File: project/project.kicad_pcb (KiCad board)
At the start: 2 copper layers, 84 x 84 mm, 155 parts, among them J101 OUT, J102 IN, J103 FFC, J104 Back, J105 Front, J301 5V, J302 24V, J303 3V3, J401 USB_C_Receptacle_USB2.0, Q101 DTC143Z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

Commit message: routing somewhat done
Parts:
- added C203: 10u/50v, Capacitor_SMD:C_0805_2012Metric_Pad1.18x1.45mm_HandSolder, F.Cu at (190.7, 103.3)
- added C205: 10u/50v, Capacitor_SMD:C_0805_2012Metric_Pad1.18x1.45mm_HandSolder, F.Cu at (139.3, 104.6)
- H101, H102: footprint MountingHole:MountingHole_3.2mm_M3_Pad_Via -> -local:MountingHole_3.2mm_M3_Pad_Via
- moved C202 55.2 mm to (188.5, 84.5), turned to -90 degrees
- moved U102 55.0 mm to (140.5, 135.6), turned to 90 degrees
- moved C201 53.3 mm to (180.5, 81.7), turned to 90 degrees
- moved R406 52.8 mm to (180.1, 140.2), turned to -90 degrees
- moved C102 52.7 mm to (143.2, 135.8), turned to -90 degrees
- moved U101 34.1 mm to (157.1, 97.6), turned to 180 degrees
- moved C101 33.5 mm to (153.9, 97.6), turned to -90 degrees
- moved kibuzzard-67570608 28.7 mm to (168.5, 122.8)
- moved R404 24.8 mm to (158.7, 124.0), turned to -90 degrees
- moved U201 19.3 mm to (194.8, 86.2), turned to 90 degrees
- moved R401 18.1 mm to (154.3, 124.0), turned to -90 degrees
- moved R402 12.4 mm to (156.3, 124.0), turned to -90 degrees
- moved R407 12.0 mm to (198.3, 125.2), turned to 90 degrees
- moved kibuzzard-66DA8205 11.4 mm to (144.3, 151.0)
- moved C204 11.0 mm to (137.9, 86.2), turned to -90 degrees
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- renumbered C203 to C204
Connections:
- C102 pad 2: B_GND -> F_GND
- C303 pad 2: B_GND -> F_GND
- C304 pad 2: B_GND -> F_GND
- C305 pad 2: B_GND -> F_GND
- C306 pad 2: B_GND -> F_GND
- C307 pad 2: B_GND -> F_GND
- C308 pad 2: B_GND -> F_GND
- C309 pad 2: B_GND -> F_GND
- C310 pad 2: B_GND -> F_GND
- C313 pad 2: B_GND -> F_GND
- C314 pad 2: B_GND -> F_GND
- C315 pad 2: B_GND -> F_GND
- C316 pad 2: B_GND -> F_GND
- C401 pad 1: B_GND -> F_GND
- C402 pad 1: B_GND -> F_GND
- C403 pad 2: B_GND -> F_GND
- C404 pad 2: B_GND -> F_GND
- C405 pad 2: B_GND -> F_GND
- C406 pad 2: B_GND -> F_GND
- C407 pad 2: B_GND -> F_GND
- C408 pad 2: B_GND -> F_GND
- C409 pad 1: B_GND -> F_GND
- C410 pad 1: B_GND -> F_GND
- C411 pad 2: B_GND -> F_GND
- C412 pad 2: B_GND -> F_GND
- C413 pad 2: B_GND -> F_GND
- H101 pad 1: unconnected-(H101-Pad1) -> F_GND
- H102 pad 1: unconnected-(H102-Pad1) -> F_GND
- H103 pad 1: unconnected-(H103-Pad1) -> F_GND
- H104 pad 1: unconnected-(H104-Pad1) -> F_GND
- J101 pad 2: B_GND -> F_GND
- J102 pad 2: B_GND -> F_GND
- J103 pad MP: GND -> F_GND
- J104 pad 1: unconnected-(J104-Pad1) -> B_SDA
- J104 pad 10: unconnected-(J104-Pad10) -> F_GND
- J104 pad 12: unconnected-(J104-Pad12) -> B_CLOCK
- J104 pad 13: unconnected-(J104-Pad13) -> B_LATCH
- J104 pad 14: unconnected-(J104-Pad14) -> B_5V
- J104 pad 15: unconnected-(J104-Pad15) -> B_CAN_LED
- J104 pad 16: unconnected-(J104-Pad16) -> B_24V
- J104 pad 2: unconnected-(J104-Pad2) -> B_3V3
- J104 pad 3: unconnected-(J104-Pad3) -> B_SCL
- J104 pad 4: unconnected-(J104-Pad4) -> F_GND
- J104 pad 6: unconnected-(J104-Pad6) -> F_GND
- J104 pad 8: unconnected-(J104-Pad8) -> B_DATA
- J105 pad 1: unconnected-(J105-Pad1) -> F_SDA
- J105 pad 10: unconnected-(J105-Pad10) -> F_GND
- J105 pad 12: unconnected-(J105-Pad12) -> F_CLOCK
- J105 pad 13: unconnected-(J105-Pad13) -> F_LATCH
- J105 pad 14: unconnected-(J105-Pad14) -> F_5V
- J105 pad 15: unconnected-(J105-Pad15) -> F_CAN_LED
- J105 pad 16: unconnected-(J105-Pad16) -> F_24V
- J105 pad 2: unconnected-(J105-Pad2) -> F_3V3
- J105 pad 3: unconnected-(J105-Pad3) -> F_SCL
- J105 pad 4: unconnected-(J105-Pad4) -> F_GND
- J105 pad 6: unconnected-(J105-Pad6) -> F_GND
- J105 pad 8: unconnected-(J105-Pad8) -> F_DATA
- J301 pad 1: B_GND -> F_GND
- J302 pad 1: B_GND -> F_GND
- J303 pad 1: B_GND -> F_GND
- J401 pad A1: B_GND -> F_GND
- J401 pad A12: B_GND -> F_GND
- J401 pad B1: B_GND -> F_GND
- J401 pad B12: B_GND -> F_GND
- J401 pad S1: B_GND -> F_GND
- R306 pad 1: B_GND -> F_GND
- R307 pad 2: B_GND -> F_GND
- R308 pad 2: B_GND -> F_GND
- R309 pad 2: B_GND -> F_GND
- R310 pad 2: B_GND -> F_GND
- R311 pad 2: B_GND -> F_GND
- R315 pad 1: B_GND -> F_GND
- R316 pad 1: B_GND -> F_GND
- R405 pad 1: B_GND -> F_GND
- R409 pad 2: B_GND -> F_GND
- R411 pad 1: B_GND -> F_GND
- SW401 pad 2: B_GND -> F_GND
- SW402 pad 2: B_GND -> F_GND
- U102 pad 2: B_GND -> F_GND
- U301 pad 2: B_GND -> F_GND
- U302 pad 2: B_GND -> F_GND
- U401 pad 33: B_GND -> F_GND
- U402 pad 2: B_GND -> F_GND
- U402 pad 8: B_GND -> F_GND
- U403 pad 2: B_GND -> F_GND
- Y401 pad 2: B_GND -> F_GND
- Y401 pad 4: B_GND -> F_GND
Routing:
- net F_24V: track 0.00 -> 143.4 mm, vias 0 -> 8
- net B_3V3: track 8.96 -> 118.3 mm, vias 0 -> 4
- net /uC/CANL: track 12.2 -> 99.2 mm, vias 0 -> 4
- net /uC/CANH: track 22.1 -> 107.1 mm, vias 0 -> 4
- net F_5V: track 0.00 -> 84.6 mm, vias 0 -> 4
- net /driver/R3: track 0.00 -> 82.8 mm, vias 0 -> 4
- net Net-(U204-Pad18): track 0.00 -> 82.4 mm, vias 0 -> 4
- net /driver/R9: track 0.00 -> 79.6 mm, vias 0 -> 4
- net Net-(U204-Pad15): track 0.00 -> 78.3 mm, vias 0 -> 2
- net Net-(U204-Pad17): track 0.00 -> 77.8 mm, vias 0 -> 4
- net Net-(U202-Pad11): track 0.00 -> 75.7 mm, vias 0 -> 6
- net /driver/R2: track 0.00 -> 74.0 mm, vias 0 -> 2
- net Net-(U204-Pad16): track 0.00 -> 73.6 mm, vias 0 -> 2
- net /driver/R10: track 0.00 -> 71.2 mm, vias 0 -> 2
- net /uC/ADC: track 0.00 -> 69.3 mm, vias 0 -> 2
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- added copper zone on F.Cu, net B_3V3
- added copper zone on B.Cu, net F_GND
- added copper zone on F.Cu, net F_GND
- removed copper zone on F.Cu, net B_GND
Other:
- copper layers 2 -> 4

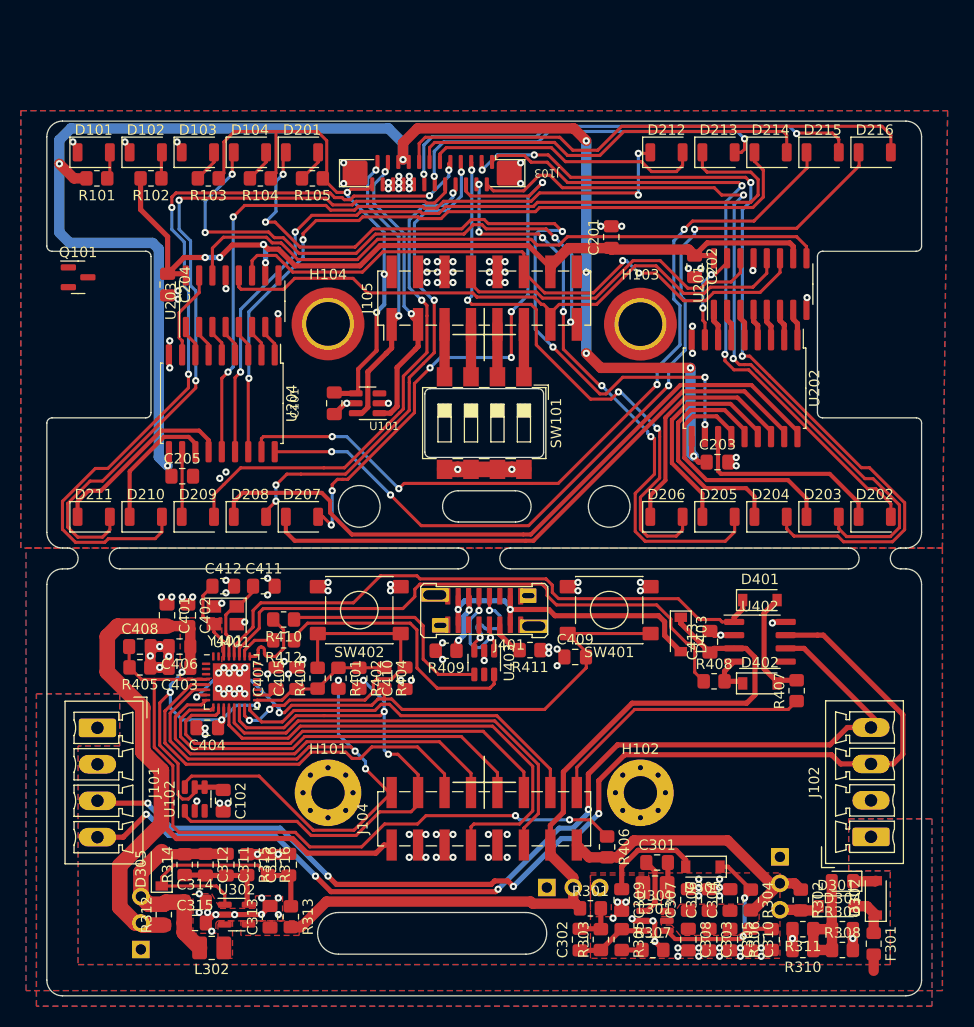
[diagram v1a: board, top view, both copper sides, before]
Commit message: fixing silk and bom and generating prod/doc files
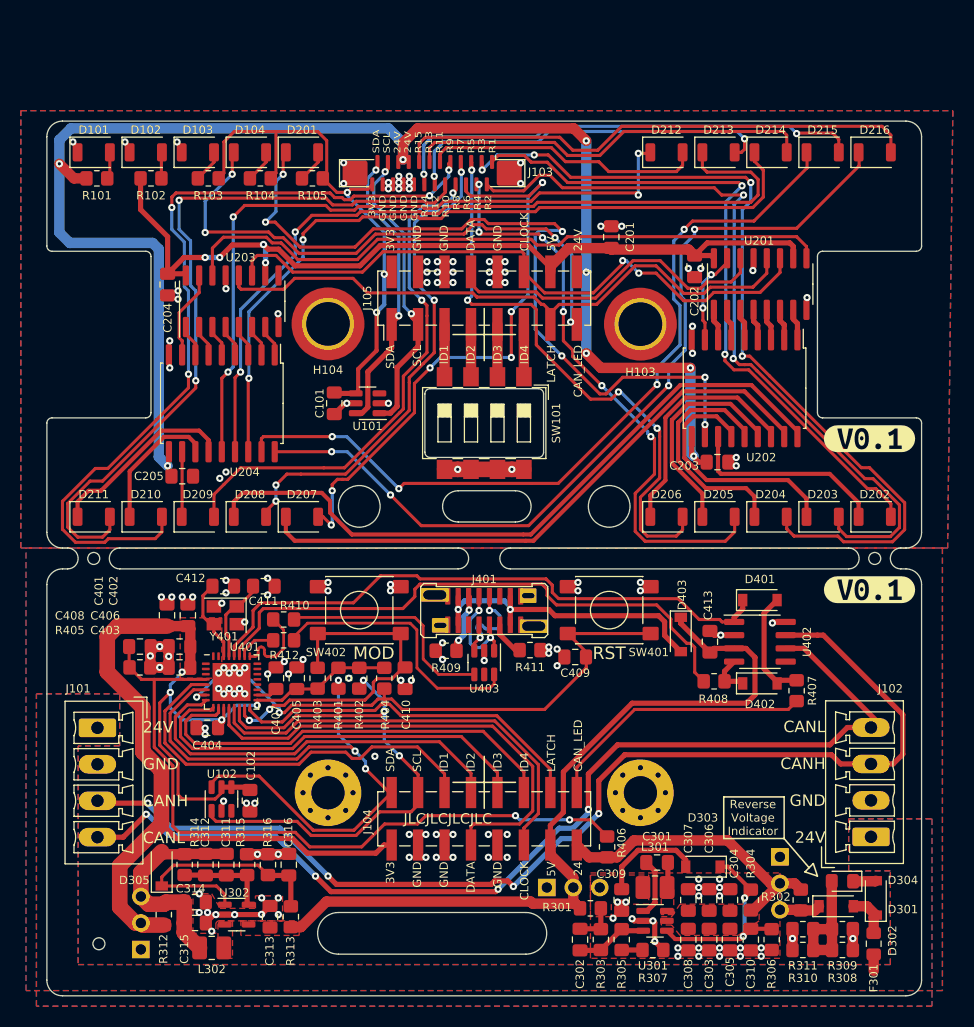
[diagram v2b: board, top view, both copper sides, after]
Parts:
- removed Q101: DTC143Z, Package_TO_SOT_SMD:SOT-23
- added REF**: toolhole, -local:toolhole, F.Cu at (205.8, 112.5)
- added REF**: toolhole, -local:toolhole, F.Cu at (130.8, 112.5)
- added REF**: toolhole, -local:toolhole, F.Cu at (131.3, 149.5)
- added kibuzzard-6761E03A: G***, kibuzzard-6761E03A, B.Cu at (168.3, 104.5)
- added kibuzzard-6761E048: G***, kibuzzard-6761E048, B.Cu at (168.3, 94.4)
- added kibuzzard-6761E1E4: G***, kibuzzard-6761E1E4, F.Cu at (205.3, 101.0)
- added kibuzzard-6761E1E4: G***, kibuzzard-6761E1E4, F.Cu at (205.3, 115.5)
- D101: value 24V -> RED
- D102: value 5V -> RED
- D103: value 3V3 -> RED
- D104: value CAN -> RED
- J101: value OUT -> BUS
- J102: value IN -> BUS
- U401: footprint Package_DFN_QFN:QFN-32-1EP_5x5mm_P0.5mm_EP3.6x3.6mm -> Package_DFN_QFN:QFN-32-1EP_5x5mm_P0.5mm_EP3.65x3.65mm
- moved G102 33.7 mm to (151.7, 97.6)
- moved G101 18.8 mm to (144.3, 97.8)
- moved C102 2.57 mm to (145.8, 135.8)
- moved U102 2.57 mm to (143.0, 135.6)
- moved G*** 1.10 mm to (168.3, 79.4)
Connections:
- net Net-(U201-Pad9) renamed /driver/O_DATA
- C102 pad 2: F_GND -> B_GND
- C303 pad 2: F_GND -> B_GND
- C304 pad 2: F_GND -> B_GND
- C305 pad 2: F_GND -> B_GND
- C306 pad 2: F_GND -> B_GND
- C307 pad 2: F_GND -> B_GND
- C308 pad 2: F_GND -> B_GND
- C309 pad 2: F_GND -> B_GND
- C310 pad 2: F_GND -> B_GND
- C313 pad 2: F_GND -> B_GND
- C314 pad 2: F_GND -> B_GND
- C315 pad 2: F_GND -> B_GND
- C316 pad 2: F_GND -> B_GND
- C401 pad 1: F_GND -> B_GND
- C402 pad 1: F_GND -> B_GND
- C403 pad 2: F_GND -> B_GND
- C404 pad 2: F_GND -> B_GND
- C405 pad 2: F_GND -> B_GND
- C406 pad 2: F_GND -> B_GND
- C407 pad 2: F_GND -> B_GND
- C408 pad 2: F_GND -> B_GND
- C409 pad 1: F_GND -> B_GND
- C410 pad 1: F_GND -> B_GND
- C411 pad 2: F_GND -> B_GND
- C412 pad 2: F_GND -> B_GND
- C413 pad 2: F_GND -> B_GND
- H101 pad 1: F_GND -> B_GND
- H102 pad 1: F_GND -> B_GND
- J101 pad 2: F_GND -> B_GND
- J102 pad 2: F_GND -> B_GND
- J104 pad 10: F_GND -> B_GND
- J104 pad 4: F_GND -> B_GND
- J104 pad 6: F_GND -> B_GND
- J301 pad 1: F_GND -> B_GND
- J302 pad 1: F_GND -> B_GND
- J303 pad 1: F_GND -> B_GND
- J401 pad A1: F_GND -> B_GND
- J401 pad A12: F_GND -> B_GND
- J401 pad B1: F_GND -> B_GND
- J401 pad B12: F_GND -> B_GND
- J401 pad S1: F_GND -> B_GND
- R306 pad 1: F_GND -> B_GND
- R307 pad 2: F_GND -> B_GND
- R308 pad 2: F_GND -> B_GND
- R309 pad 2: F_GND -> B_GND
- R310 pad 2: F_GND -> B_GND
- R311 pad 2: F_GND -> B_GND
- R315 pad 1: F_GND -> B_GND
- R316 pad 1: F_GND -> B_GND
- R405 pad 1: F_GND -> B_GND
- R409 pad 2: F_GND -> B_GND
- R411 pad 1: F_GND -> B_GND
- SW401 pad 2: F_GND -> B_GND
- SW402 pad 2: F_GND -> B_GND
- U102 pad 2: F_GND -> B_GND
- U301 pad 2: F_GND -> B_GND
- U302 pad 2: F_GND -> B_GND
- U401 pad 33: F_GND -> B_GND
- U402 pad 2: F_GND -> B_GND
- U402 pad 8: F_GND -> B_GND
- U403 pad 2: F_GND -> B_GND
- Y401 pad 2: F_GND -> B_GND
- Y401 pad 4: F_GND -> B_GND
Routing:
- net F_GND: track 45.2 -> 11.0 mm, vias 154 -> 52
- net B_GND: track 0.00 -> 34.2 mm, vias 0 -> 104
- net B_SCL: track 56.6 -> 53.6 mm
- net B_SDA: track 64.2 -> 61.6 mm
- net B_3V3: track 118.3 -> 120.9 mm
- added copper zone on B.Cu, net B_GND
- added copper zone on F.Cu, net B_GND
- added copper zone on In1.Cu, net B_GND
- added copper zone on In2.Cu, net B_GND
- added copper zone on In1.Cu, net F_GND
- added copper zone on In2.Cu, net F_GND
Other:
- board text added: "3V3 GND GND DATA GND CLOCK 5V 24"
- board text added: "3V3 GND GND DATA GND CLOCK 5V 24V"
- board text added: "3V3 GND GND GND GND R14 R12 R10 R8 R6 R4 R2"
- board text added: "JLCJLCJLCJLC"
- board text added: "MOD"
- board text added: "RST"
- board text added: "Reverse Voltage Indicator"
- board text added: "SDA SCL 24V 24V R15 R13 R11 R9 R7 R5 R3 R1"
- board text added: "SDA SCL ID1 ID2 ID3 ID4 LATCH CAN_LED"

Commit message: bom fixes
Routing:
- net Net-(D203-Pad1): track 24.2 -> 24.8 mm
- net F_GND: vias 52 -> 51
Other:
- board text added: "Layers: 4 (stackup: JLC04161H-7628)"
